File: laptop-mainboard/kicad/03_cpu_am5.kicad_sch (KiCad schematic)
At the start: 3 parts, among them U19 W25Q256JW_BIOS, Y1 XTAL_32K768

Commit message: Rev B: echte AM5-Pinbelegung, Kleinteile, EliteBook-850-G7-Format
- AM5-Pinmap (1718 Pins, WikiChip/Wikimedia Public Domain) als CSV,
  Sockel-Footprint mit echten Padnamen und 1708 Signal-Netzen im Board
- Blatt 10: MLCC-Baenke, 11 ESD-Arrays, USB2-Chokes, Straps; 48-MHz-Quarz;
  beidseitige Bestueckung (B.Cu) mit Kollisionspruefung pro Seite
- Board 340x112mm im EliteBook-850-G7-Layout: USB-C-100W-PD an der
  Barrel-Jack-Position, TB4/HDMI/USB-A/RJ45 rechts, USB-A/Klinke links,
  HP-Akku 3S/56Wh, HP-FPC-Steckplaetze (Pinouts zu verifizieren)
- GND-Stitching-Vias, MDI-/DP-Korridore, 645 Board-Netze
- Renderer tools/render_board.py erzeugt docs/board_render.png
- Doku: elitebook.md neu, grenzen.md/README/power/layout aktualisiert

Co-Authored-By: Claude Fable 5 <noreply@anthropic.com>
Claude-Session: https://claude.ai/code/session_01E8mU1RUAv938Hs69waADCc
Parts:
- added Y2: XTAL_48M, laptop_mainboard:XTAL_3225, symbol lm:XTAL_48M_Y2
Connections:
- net LAN2_CLKREQ# is gone; now on net TB_CLKREQ#: XU1.81 (CLKREQ2#)
- net LAN2_PE_TXN is gone; now on net LAN1_PE_RXN: XU1.68 (G0_RXN)
- net LAN2_PE_TXP is gone; now on net LAN1_PE_RXP: XU1.67 (G0_RXP)
- net SD_SS_RXN is gone; now on net TBDP0_HPD: XU1.103 (DP0_HPD)
- net SD_SS_RXP is gone; now on net TBDP0_AUXN: XU1.102 (DP0_AUXN)
- net SD_SS_TXN is gone; now on net TBDP0_AUXP: XU1.101 (DP0_AUXP)
- net SD_SS_TXP is gone; now on net TBDP0_TXN[3:0]: XU1.100 (DP0_TXN[3:0])
- net USB2_N[9:1] is gone; now on net TBDP1_TXN[3:0]: XU1.105 (DP1_TXN[3:0])
- net USB2_P[9:1] is gone; now on net TBDP1_TXP[3:0]: XU1.104 (DP1_TXP[3:0])
- net USBC2_TXN is gone; now on net USBA2_RXN: XU1.93 (U3G2_2_RXN)
- net USBC2_TXP is gone; now on net USBA2_RXP: XU1.92 (U3G2_2_RXP)
- net USBC3_RXN is gone; now on net TBDP0_TXP[3:0]: XU1.99 (DP0_TXP[3:0])
- net EDP_AUXN: now also XU1.124 (EDP_AUXN); no longer XU1.131 (EDP_AUXN)
- net EDP_AUXP: now also XU1.123 (EDP_AUXP); no longer XU1.130 (EDP_AUXP)
- net EDP_HPD: now also XU1.125 (EDP_HPD); no longer XU1.132 (EDP_HPD)
- net EDP_TXN[1:0]: now also XU1.122 (EDP_TXN[1:0]); no longer XU1.129 (EDP_TXN[1:0])
- net EDP_TXP[1:0]: now also XU1.121 (EDP_TXP[1:0]); no longer XU1.128 (EDP_TXP[1:0])
- net HDA_BCLK: now also XU1.126 (HDA_BCLK); no longer XU1.133 (HDA_BCLK)
- net HDA_RST#: now also XU1.130 (HDA_RST#); no longer XU1.137 (HDA_RST#)
- net HDA_SDI: now also XU1.129 (HDA_SDI); no longer XU1.136 (HDA_SDI)
- net HDA_SDO: now also XU1.128 (HDA_SDO); no longer XU1.135 (HDA_SDO)
- net HDA_SYNC: now also XU1.127 (HDA_SYNC); no longer XU1.134 (HDA_SYNC)
- net HDMI_CEC: now also XU1.119 (HDMI_CEC); no longer XU1.126 (HDMI_CEC)
- net HDMI_CLKN: now also XU1.116 (HDMI_CLKN); no longer XU1.123 (HDMI_CLKN)
- net HDMI_CLKP: now also XU1.115 (HDMI_CLKP); no longer XU1.122 (HDMI_CLKP)
- net HDMI_D0N: now also XU1.114 (HDMI_D0N); no longer XU1.121 (HDMI_D0N)
- net HDMI_D0P: now also XU1.113 (HDMI_D0P); no longer XU1.120 (HDMI_D0P)
- net HDMI_D1N: now also XU1.112 (HDMI_D1N); no longer XU1.119 (HDMI_D1N)
- net HDMI_D1P: now also XU1.111 (HDMI_D1P); no longer XU1.118 (HDMI_D1P)
- net HDMI_D2N: now also XU1.110 (HDMI_D2N); no longer XU1.117 (HDMI_D2N)
- net HDMI_D2P: now also XU1.109 (HDMI_D2P); no longer XU1.116 (HDMI_D2P)
- net HDMI_HPD: now also XU1.120 (HDMI_HPD); no longer XU1.127 (HDMI_HPD)
- net HDMI_SCL: now also XU1.117 (HDMI_SCL); no longer XU1.124 (HDMI_SCL)
- net HDMI_SDA: now also XU1.118 (HDMI_SDA); no longer XU1.125 (HDMI_SDA)
- net LAN1_CLKREQ#: now also XU1.82 (CLKREQ3#); no longer XU1.80 (CLKREQ3#)
- net LAN1_PE_RXN: no longer XU1.66 (G0_RXN)
- net LAN1_PE_RXP: no longer XU1.65 (G0_RXP)
- net LAN1_PE_TXN: now also XU1.66 (G0_TXN); no longer XU1.64 (G0_TXN)
- net LAN1_PE_TXP: now also XU1.65 (G0_TXP); no longer XU1.63 (G0_TXP)
- net NVME1_CLKREQ#: now also XU1.79 (CLKREQ0#); no longer XU1.77 (CLKREQ0#)
- net NVME1_RXN[3:0]: now also XU1.56 (P0_RXN[3:0]); no longer XU1.54 (P0_RXN[3:0])
- net NVME1_RXP[3:0]: now also XU1.55 (P0_RXP[3:0]); no longer XU1.53 (P0_RXP[3:0])
- net NVME1_TXN[3:0]: now also XU1.54 (P0_TXN[3:0]); no longer XU1.52 (P0_TXN[3:0])
- net NVME1_TXP[3:0]: now also XU1.53 (P0_TXP[3:0]); no longer XU1.51 (P0_TXP[3:0])
- net NVME2_CLKREQ#: now also XU1.80 (CLKREQ1#); no longer XU1.78 (CLKREQ1#)
- net NVME2_RXN[3:0]: now also XU1.60 (P1_RXN[3:0]); no longer XU1.58 (P1_RXN[3:0])
- net NVME2_RXP[3:0]: now also XU1.59 (P1_RXP[3:0]); no longer XU1.57 (P1_RXP[3:0])
- net NVME2_TXN[3:0]: now also XU1.58 (P1_TXN[3:0]); no longer XU1.56 (P1_TXN[3:0])
- net NVME2_TXP[3:0]: now also XU1.57 (P1_TXP[3:0]); no longer XU1.55 (P1_TXP[3:0])
- net PE_CLKN[5:0]: now also XU1.78 (GPP_CLKN[5:0]); no longer XU1.76 (GPP_CLKN[5:0])
- net PE_CLKP[5:0]: now also XU1.77 (GPP_CLKP[5:0]); no longer XU1.75 (GPP_CLKP[5:0])
- net PE_WAKE#: now also XU1.85 (PE_WAKE#); no longer XU1.83 (PE_WAKE#)
- net TBDP0_AUXN: no longer XU1.109 (DP0_AUXN)
- net TBDP0_AUXP: no longer XU1.108 (DP0_AUXP)
- net TBDP0_HPD: no longer XU1.110 (DP0_HPD)
- net TBDP0_TXN[3:0]: no longer XU1.107 (DP0_TXN[3:0])
- net TBDP0_TXP[3:0]: no longer XU1.106 (DP0_TXP[3:0])
- net TBDP1_AUXN: now also XU1.107 (DP1_AUXN); no longer XU1.114 (DP1_AUXN)
- net TBDP1_AUXP: now also XU1.106 (DP1_AUXP); no longer XU1.113 (DP1_AUXP)
- net TBDP1_HPD: now also XU1.108 (DP1_HPD); no longer XU1.115 (DP1_HPD)
- net TBDP1_TXN[3:0]: no longer XU1.112 (DP1_TXN[3:0])
- net TBDP1_TXP[3:0]: no longer XU1.111 (DP1_TXP[3:0])
- net TB_CLKREQ#: no longer XU1.79 (CLKREQ2#)
- net TB_RXN[3:0]: now also XU1.64 (P2_RXN[3:0]); no longer XU1.62 (P2_RXN[3:0])
- net TB_RXP[3:0]: now also XU1.63 (P2_RXP[3:0]); no longer XU1.61 (P2_RXP[3:0])
- net TB_TXN[3:0]: now also XU1.62 (P2_TXN[3:0]); no longer XU1.60 (P2_TXN[3:0])
- net TB_TXP[3:0]: now also XU1.61 (P2_TXP[3:0]); no longer XU1.59 (P2_TXP[3:0])
- net USBA1_RXN: now also XU1.89 (U3G2_1_RXN); no longer XU1.87 (U3G2_1_RXN)
- net USBA1_RXP: now also XU1.88 (U3G2_1_RXP); no longer XU1.86 (U3G2_1_RXP)
- net USBA1_TXN: now also XU1.87 (U3G2_1_TXN); no longer XU1.85 (U3G2_1_TXN)
- net USBA1_TXP: now also XU1.86 (U3G2_1_TXP); no longer XU1.84 (U3G2_1_TXP)
- net USBA2_RXN: no longer XU1.91 (U3G2_2_RXN)
- net USBA2_RXP: no longer XU1.90 (U3G2_2_RXP)
- net USBA2_TXN: now also XU1.91 (U3G2_2_TXN); no longer XU1.89 (U3G2_2_TXN)
- net USBA2_TXP: now also XU1.90 (U3G2_2_TXP); no longer XU1.88 (U3G2_2_TXP)
- net WIFI_CLKREQ#: now also XU1.84 (CLKREQ5#); no longer XU1.82 (CLKREQ5#)
- net WIFI_PE_RXN: now also XU1.76 (G2_RXN); no longer XU1.74 (G2_RXN)
- net WIFI_PE_RXP: now also XU1.75 (G2_RXP); no longer XU1.73 (G2_RXP)
- net WIFI_PE_TXN: now also XU1.74 (G2_TXN); no longer XU1.72 (G2_TXN)
- net WIFI_PE_TXP: now also XU1.73 (G2_TXP); no longer XU1.71 (G2_TXP)
- net LAN2_PE_RXN: no longer names the net of XU1.70 (G1_TXN)
- net LAN2_PE_RXP: no longer names the net of XU1.69 (G1_TXP)
- net USBC2_RXN: no longer names the net of XU1.95 (U3G2_4)
- net USBC2_RXP: no longer names the net of XU1.94 (U3G2_3)
- net USBC3_RXP renamed USB2_N[8:1]
- net USBC3_TXN renamed USB2_P[8:1]
- net USBC3_TXP: no longer names the net of XU1.96 (U3G1_5)
- new net X48M_OSC: XU1.52 (X48M_OSC), Y2.2 (OSC)
- new net X48M_X1: XU1.51 (X48M_X1), Y2.1 (X1)
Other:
- note added: "(Quelle: WikiChip via Wikimedia Commons, Public Domain)."
- note added: "Footprint-Pads tragen die echten Signal-Netznamen."
- note added: "PCIe Gen4 Lane-Budget: 2x4 NVMe, x4 TB4, 2x1 (LAN, WLAN)."
- note added: "Pinbelegung aller 1718 Pads: docs/am5_pinmap.csv"
- note removed: "PCIe Gen4 Lane-Budget: 2x4 NVMe, x4 TB4, 3x1 (2x LAN, WLAN)."
- note removed: "Pinsymbol funktional gruppiert - vollstaendige Ballout-Zuordnung"
- note removed: "erfordert AMD-NDA-Dokumentation (siehe docs/grenzen.md)."

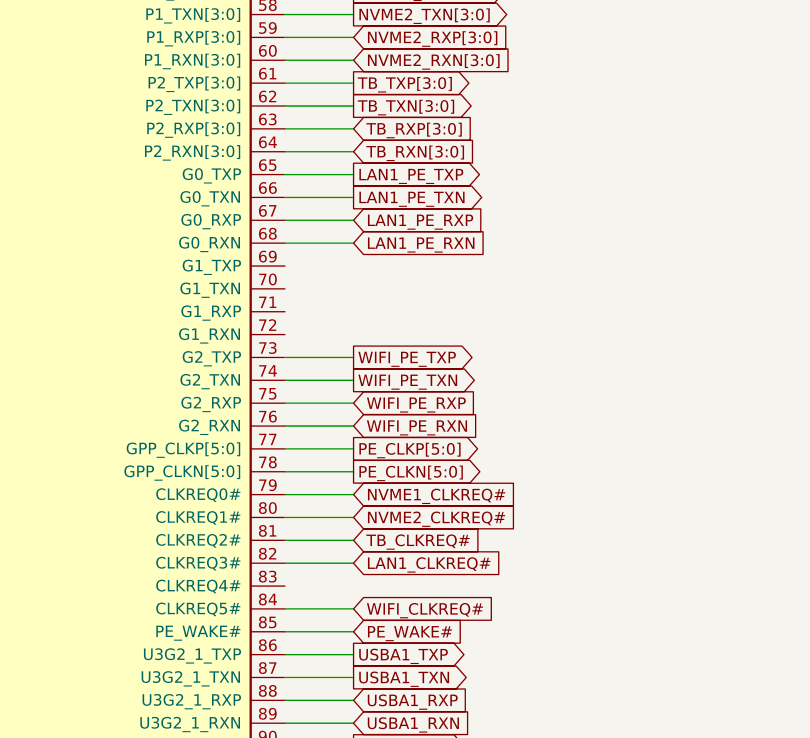
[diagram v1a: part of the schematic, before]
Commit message: Portlayout nach Fotos des Originalgeraets korrigiert
- Rechte Kante hinten->vorn: USB-C-Ladeport 100W (Barrel-Position,
  eigener TPS65987D + Config-Flash, neues Blatt 07_ladeport), USB-A,
  HDMI, 2x USB-C Thunderbolt 4 nebeneinander (JHL8540)
- Kein RJ45 (Original hat keines): Ethernet entfernt, G0/G1 Reserve
- TPS65988 nur noch Source fuer die TB-Ports; breite VBUS_IN-Trasse
  vom Ladeport zum BQ25731
- Interne Anschlusspositionen des Original-Mainboards (Nutzerfoto)
  als Referenztabelle in docs/elitebook.md dokumentiert
- Doku, Blockdiagramm, BOM und Rendering aktualisiert

Co-Authored-By: Claude Fable 5 <noreply@anthropic.com>
Claude-Session: https://claude.ai/code/session_01E8mU1RUAv938Hs69waADCc
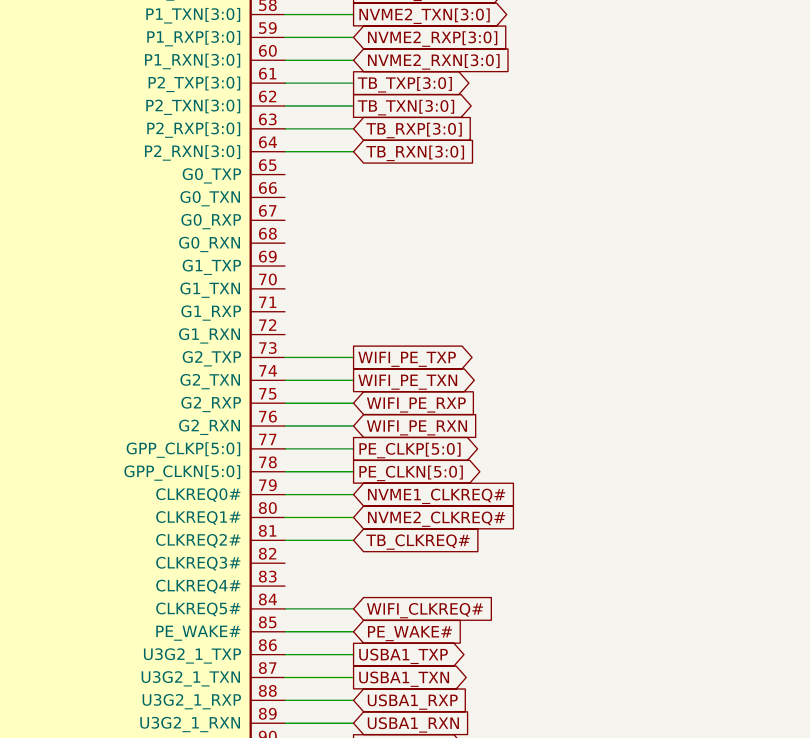
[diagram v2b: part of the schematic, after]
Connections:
- net LAN1_CLKREQ#: no longer names the net of XU1.82 (CLKREQ3#)
- net LAN1_PE_RXN: no longer names the net of XU1.68 (G0_RXN)
- net LAN1_PE_RXP: no longer names the net of XU1.67 (G0_RXP)
- net LAN1_PE_TXN: no longer names the net of XU1.66 (G0_TXN)
- net LAN1_PE_TXP: no longer names the net of XU1.65 (G0_TXP)
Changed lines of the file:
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@@
     (property "Intersheetrefs" "${INTERSHEET_REFS}" (at 159.37 74.93 0) (effects (font (size 1.27 1.27)) (hide yes)))
-  )
-  (wire (pts (xy 151.75 77.47) (xy 159.37 77.47)) (stroke (width 0) (type default)))
-  (global_label "LAN1_PE_TXP" (shape output) (at 159.37 77.47 0) (fields_autoplaced yes)
-    (effects (font (size 1.27 1.27)) (justify left))
-    (property "Intersheetrefs" "${INTERSHEET_REFS}" (at 159.37 77.47 0) (effects (font (size 1.27 1.27)) (hide yes)))
-  )
-  (wire (pts (xy 151.75 80.01) (xy 159.37 80.01)) (stroke (width 0) (type default)))
-  (global_label "LAN1_PE_TXN" (shape output) (at 159.37 80.01 0) (fields_autoplaced yes)
-    (effects (font (size 1.27 1.27)) (justify left))
-    (property "Intersheetrefs" "${INTERSHEET_REFS}" (at 159.37 80.01 0) (effects (font (size 1.27 1.27)) (hide yes)))
-  )
-  (wire (pts (xy 151.75 82.55) (xy 159.37 82.55)) (stroke (width 0) (type default)))
-  (global_label "LAN1_PE_RXP" (shape input) (at 159.37 82.55 0) (fields_autoplaced yes)
-    (effects (font (size 1.27 1.27)) (justify left))
-    (property "Intersheetrefs" "${INTERSHEET_REFS}" (at 159.37 82.55 0) (effects (font (size 1.27 1.27)) (hide yes)))
-  )
-  (wire (pts (xy 151.75 85.09) (xy 159.37 85.09)) (stroke (width 0) (type default)))
-  (global_label "LAN1_PE_RXN" (shape input) (at 159.37 85.09 0) (fields_autoplaced yes)
-    (effects (font (size 1.27 1.27)) (justify left))
-    (property "Intersheetrefs" "${INTERSHEET_REFS}" (at 159.37 85.09 0) (effects (font (size 1.27 1.27)) (hide yes)))
   )
   (wire (pts (xy 151.75 97.79) (xy 159.37 97.79)) (stroke (width 0) (type default)))
@@
     (property "Intersheetrefs" "${INTERSHEET_REFS}" (at 159.37 118.11 0) (effects (font (size 1.27 1.27)) (hide yes)))
   )
-  (wire (pts (xy 151.75 120.65) (xy 159.37 120.65)) (stroke (width 0) (type default)))
-  (global_label "LAN1_CLKREQ#" (shape input) (at 159.37 120.65 0) (fields_autoplaced yes)
-    (effects (font (size 1.27 1.27)) (justify left))
-    (property "Intersheetrefs" "${INTERSHEET_REFS}" (at 159.37 120.65 0) (effects (font (size 1.27 1.27)) (hide yes)))
-  )
   (wire (pts (xy 151.75 125.73) (xy 159.37 125.73)) (stroke (width 0) (type default)))
